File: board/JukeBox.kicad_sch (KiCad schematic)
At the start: 41 parts, among them J1 USB_C_Receptacle_USB2.0, J2 Conn_01x02, J3 Conn_01x04, J4 Conn_01x03, SW1 SW_SPST, SW10 SW_SPST, SW11 SW_SPST, SW12 SW_SPST, SW2 SW_SPST, SW3 SW_SPST, SW4 SW_SPST, SW5 SW_SPST, SW6 SW_SPST, SW7 SW_SPST, SW8 SW_SPST, SW9 SW_SPST, U1 ATmega8U2-A, Y1 16MHz

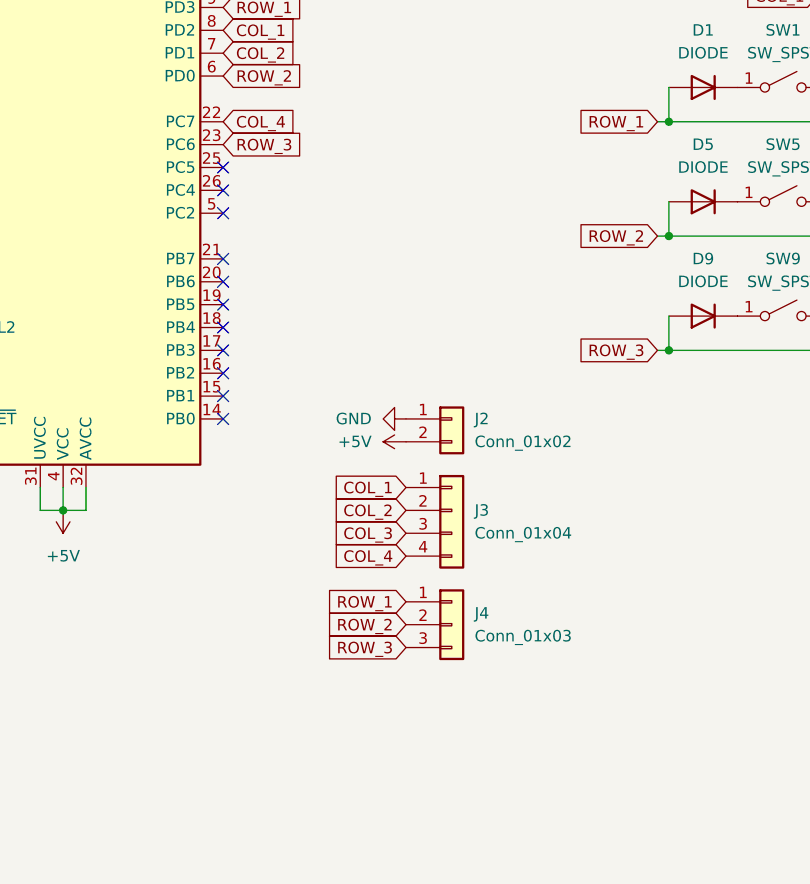
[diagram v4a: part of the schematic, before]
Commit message: add footprint for screen addon, change all tht components to smt
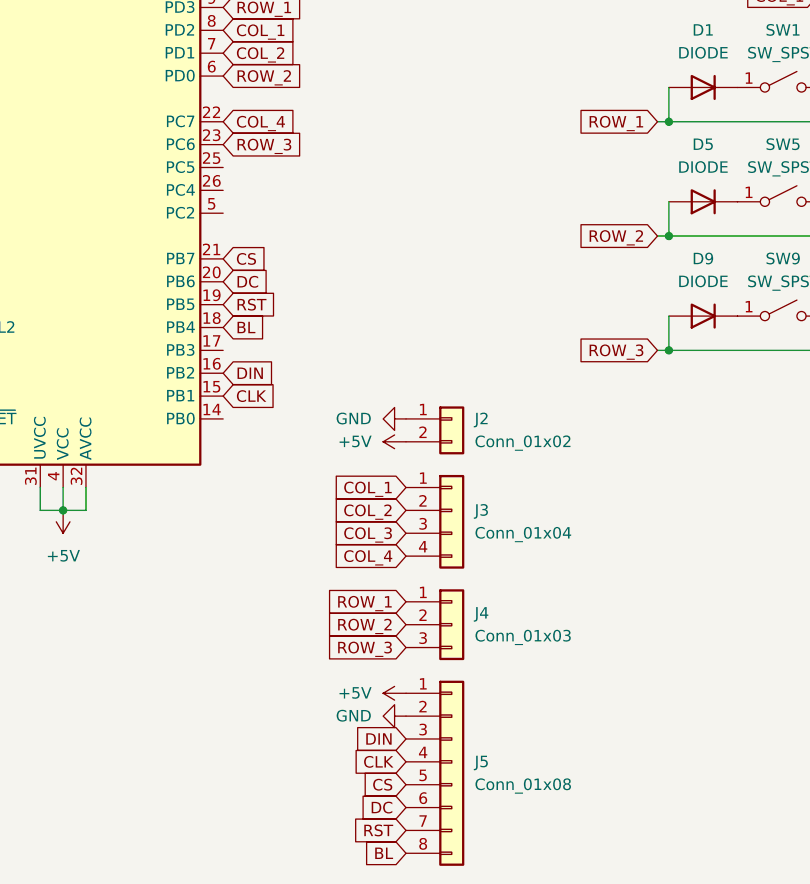
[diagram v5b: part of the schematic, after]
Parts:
- added J5: Conn_01x08, Connector_PinHeader_2.54mm:PinHeader_1x08_P2.54mm_Vertical, symbol Connector_Generic:Conn_01x08
- C1, C2, C3: footprint Capacitor_THT:C_Disc_D5.0mm_W2.5mm_P5.00mm -> Capacitor_SMD:C_1206_3216Metric_Pad1.33x1.80mm_HandSolder
- D1, D10, D11, D12, D2, D3, D4, D5, D6, D7, D8, D9: footprint Diode_THT:D_DO-15_P10.16mm_Horizontal -> Diode_SMD:D_1206_3216Metric_Pad1.42x1.75mm_HandSolder
- R1, R10, R11, R12, R2, R3, R4: footprint Resistor_THT:R_Axial_DIN0207_L6.3mm_D2.5mm_P10.16mm_Horizontal -> Resistor_SMD:R_1206_3216Metric_Pad1.30x1.75mm_HandSolder
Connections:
- net +5V: now also J5.1 (Pin_1)
- net GND: now also J5.2 (Pin_2)
- net CLK: now reaches U1.15 (PB1)
- net CLK: now also J5.4 (Pin_4)
- net DIN: now reaches U1.16 (PB2)
- net DIN: now also J5.3 (Pin_3)
- net BL: now reaches U1.18 (PB4)
- net BL: now also J5.8 (Pin_8)
- net RST: now reaches U1.19 (PB5)
- net RST: now also J5.7 (Pin_7)
- net DC: now reaches U1.20 (PB6)
- net DC: now also J5.6 (Pin_6)
- net CS: now reaches U1.21 (PB7)
- net CS: now also J5.5 (Pin_5)
- no-connect marks 16 -> 5

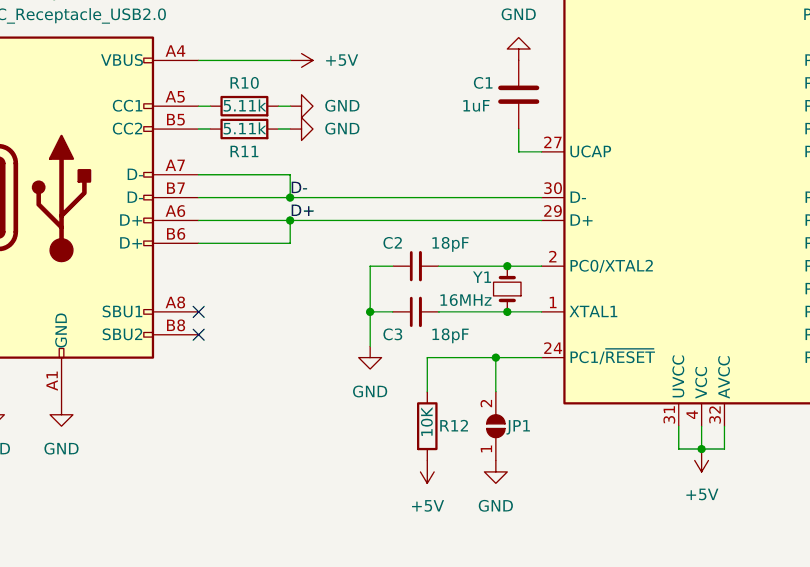
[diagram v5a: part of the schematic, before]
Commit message: add resistors to schematic, add mcu programming docs, add star to platformio stuff for atmega8u2
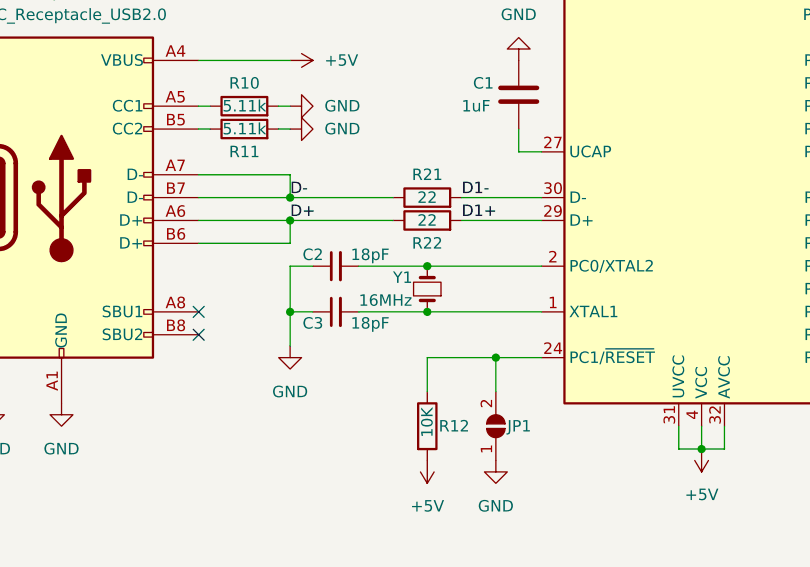
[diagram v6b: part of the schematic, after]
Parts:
- added R21, R22: 22, Resistor_SMD:R_1206_3216Metric_Pad1.30x1.75mm_HandSolder, symbol Device:R
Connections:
- net D+: now also R22.1; no longer U1.29 (D+)
- net D-: now also R21.1; no longer U1.30 (D-)
- new net D1+: R22.2, U1.29 (D+)
- new net D1-: R21.2, U1.30 (D-)
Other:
- moved on the sheet: C2, C3, Y1

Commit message: import rp2040 minimal kicad project
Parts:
- removed C2, C3: 18pF, Capacitor_SMD:C_1206_3216Metric_Pad1.33x1.80mm_HandSolder, symbol Device:C_Small
- removed D1, D10, D11, D12, D2, D3, D4, D5, D6, D7, D8, D9: DIODE, Diode_SMD:D_1206_3216Metric_Pad1.42x1.75mm_HandSolder, symbol Simulation_SPICE:DIODE
- removed J1: USB_C_Receptacle_USB2.0, jukebox-footprints:GCT_USB4085-GF-A_REVA4, symbol Connector:USB_C_Receptacle_USB2.0
- removed J3: Conn_01x04, Connector_PinHeader_2.54mm:PinHeader_1x04_P2.54mm_Vertical, symbol Connector_Generic:Conn_01x04
- removed J4: Conn_01x03, Connector_PinHeader_2.54mm:PinHeader_1x03_P2.54mm_Vertical, symbol Connector_Generic:Conn_01x03
- removed J5: Conn_01x08, Connector_PinHeader_2.54mm:PinHeader_1x08_P2.54mm_Vertical, symbol Connector_Generic:Conn_01x08
- removed JP1: (no value), Jumper:SolderJumper-2_P1.3mm_Open_Pad1.0x1.5mm, symbol Jumper:SolderJumper_2_Open
- removed R10, R11: 5.11k, Resistor_SMD:R_1206_3216Metric_Pad1.30x1.75mm_HandSolder, symbol Device:R
- removed R12: 10K, Resistor_SMD:R_1206_3216Metric_Pad1.30x1.75mm_HandSolder, symbol Device:R
- removed R21, R22: 22, Resistor_SMD:R_1206_3216Metric_Pad1.30x1.75mm_HandSolder, symbol Device:R
- removed SW1, SW10, SW11, SW12, SW2, SW3, SW4, SW5, SW6, SW7, SW8, SW9: SW_SPST, jukebox-footprints:Kailh_PG1350, symbol Switch:SW_SPST
- removed U1: ATmega8U2-A, Package_QFP:TQFP-32_7x7mm_P0.8mm, symbol MCU_Microchip_ATmega:ATmega8U2-A
- removed Y1: 16MHz, Crystal:Crystal_HC49-4H_Vertical, symbol Device:Crystal_Small
- added C10, C11, C12, C13, C14, C15, C16, C17, C2, C3, C4, C5, C6, C7, C8, C9: (no value), symbol Device:C
- added H1, H2, H3, H4: (no value), symbol Mechanical:MountingHole
- added J1: (no value), symbol Connector:USB_B_Micro
- added J3, J4: (no value), symbol Connector_Generic:Conn_02x18_Odd_Even
- added R5: (no value), symbol Device:R
- added U1: (no value), symbol Regulator_Linear:NCP1117-3.3_SOT223
- added U2: (no value), symbol Memory_Flash:W25Q128JVS
- added U3: (no value), symbol MCU_RaspberryPi_RP2040:RP2040
- added Y1: (no value), symbol Device:Crystal
- C1: value 1uF -> (none); footprint Capacitor_SMD:C_1206_3216Metric_Pad1.33x1.80mm_HandSolder -> (none)
- J2: value Conn_01x02 -> (none); footprint Connector_PinHeader_2.54mm:PinHeader_1x02_P2.54mm_Vertical -> (none)
- R1, R2, R3, R4: value 10k -> (none); footprint Resistor_SMD:R_1206_3216Metric_Pad1.30x1.75mm_HandSolder -> (none)
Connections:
- net +5V is gone; now on net GND: J2.2 (Pin_2)
- net GND: now also C1.2, C10.2, C11.2, C12.2, C13.2, C14.2, C15.2, C16.2, C17.2, C2.2, C3.2, C4.2, C5.2, C6.2, C7.2, C8.2, C9.2, J1.5 (GND), J1.6 (Shield), J3.1 (Pin_1), J3.11 (Pin_11), J3.13 (Pin_13), J3.15 (Pin_15), J3.17 (Pin_17), J3.19 (Pin_19), J3.21 (Pin_21), J3.23 (Pin_23), J3.25 (Pin_25), J3.27 (Pin_27), J3.29 (Pin_29), J3.3 (Pin_3), J3.31 (Pin_31), J3.33 (Pin_33), J3.35 (Pin_35), J3.36 (Pin_36), J3.5 (Pin_5), J3.7 (Pin_7), J3.9 (Pin_9), J4.10 (Pin_10), J4.12 (Pin_12), J4.14 (Pin_14), J4.16 (Pin_16), J4.18 (Pin_18), J4.2 (Pin_2), J4.20 (Pin_20), J4.22 (Pin_22), J4.24 (Pin_24), J4.26 (Pin_26), J4.28 (Pin_28), J4.30 (Pin_30), J4.32 (Pin_32), J4.34 (Pin_34), J4.35 (Pin_35), J4.36 (Pin_36), J4.4 (Pin_4), J4.6 (Pin_6), J4.8 (Pin_8), U1.1 (GND), U2.4 (GND), U3.19 (TESTEN), U3.57 (GND); no longer C1.1, J2.1 (Pin_1), R1.1, R2.1, R3.1, R4.1
- net COL_1 renamed ~{USB_BOOT}
- net ~{USB_BOOT}: now also J2.1 (Pin_1)
- net COL_2 renamed QSPI_SS
- net QSPI_SS: now also R1.1, U2.1 (~{CS}), U3.56 (QSPI_SS)
- net COL_3: no longer names the net of R3.2
- net COL_3: now also U3.47 (USB_DP)
- net COL_4: no longer names the net of R4.2
- net COL_4: now also U3.46 (USB_DM)
- new net: C3.1, R5.2, Y1.2
- new net +1V1: C6.1, C7.1, C8.1, U3.23 (DVDD), U3.45 (VREG_VOUT), U3.50 (DVDD)
- new net +3V3: C10.1, C11.1, C12.1, C13.1, C14.1, C15.1, C16.1, C17.1, C4.1, C5.1, C9.1, J3.2 (Pin_2), R2.1, U1.2 (VO), U2.8 (VCC), U3.1 (IOVDD), U3.10 (IOVDD), U3.22 (IOVDD), U3.33 (IOVDD), U3.42 (IOVDD), U3.43 (ADC_AVDD), U3.44 (VREG_IN), U3.48 (USB_VDD), U3.49 (IOVDD)
- new net GPIO0: J3.4 (Pin_4), U3.2 (GPIO0)
- new net GPIO1: J3.6 (Pin_6), U3.3 (GPIO1)
- new net GPIO10: J3.24 (Pin_24), U3.13 (GPIO10)
- new net GPIO11: J3.26 (Pin_26), U3.14 (GPIO11)
- new net GPIO12: J3.28 (Pin_28), U3.15 (GPIO12)
- new net GPIO13: J3.30 (Pin_30), U3.16 (GPIO13)
- new net GPIO14: J3.32 (Pin_32), U3.17 (GPIO14)
- new net GPIO15: J3.34 (Pin_34), U3.18 (GPIO15)
- new net GPIO16: J4.27 (Pin_27), U3.27 (GPIO16)
- new net GPIO17: J4.25 (Pin_25), U3.28 (GPIO17)
- new net GPIO18: J4.23 (Pin_23), U3.29 (GPIO18)
- new net GPIO19: J4.21 (Pin_21), U3.30 (GPIO19)
- new net GPIO2: J3.8 (Pin_8), U3.4 (GPIO2)
- new net GPIO20: J4.19 (Pin_19), U3.31 (GPIO20)
- new net GPIO21: J4.17 (Pin_17), U3.32 (GPIO21)
- new net GPIO22: J4.15 (Pin_15), U3.34 (GPIO22)
- new net GPIO23: J4.13 (Pin_13), U3.35 (GPIO23)
- new net GPIO24: J4.11 (Pin_11), U3.36 (GPIO24)
- new net GPIO25: J4.9 (Pin_9), U3.37 (GPIO25)
- new net GPIO26_ADC0: J4.7 (Pin_7), U3.38 (GPIO26_ADC0)
- new net GPIO27_ADC1: J4.5 (Pin_5), U3.39 (GPIO27_ADC1)
- new net GPIO28_ADC2: J4.3 (Pin_3), U3.40 (GPIO28_ADC2)
- new net GPIO29_ADC3: J4.1 (Pin_1), U3.41 (GPIO29_ADC3)
- new net GPIO3: J3.10 (Pin_10), U3.5 (GPIO3)
- new net GPIO4: J3.12 (Pin_12), U3.6 (GPIO4)
- new net GPIO5: J3.14 (Pin_14), U3.7 (GPIO5)
- new net GPIO6: J3.16 (Pin_16), U3.8 (GPIO6)
- new net GPIO7: J3.18 (Pin_18), U3.9 (GPIO7)
- new net GPIO8: J3.20 (Pin_20), U3.11 (GPIO8)
- new net GPIO9: J3.22 (Pin_22), U3.12 (GPIO9)
- new net QSPI_SCLK: U2.6 (CLK), U3.52 (QSPI_SCLK)
- new net QSPI_SD0: U2.5 (DI(IO0)), U3.53 (QSPI_SD0)
- new net QSPI_SD1: U2.2 (DO(IO1)), U3.55 (QSPI_SD1)
- new net QSPI_SD2: U2.3 (IO2), U3.54 (QSPI_SD2)
- new net QSPI_SD3: U2.7 (IO3), U3.51 (QSPI_SD3)
- new net RUN: J4.29 (Pin_29), U3.26 (RUN)
- new net SWCLK: J4.33 (Pin_33), U3.24 (SWCLK)
- new net SWD: J4.31 (Pin_31), U3.25 (SWD)
- new net USB_D+: J1.3 (D+), R3.1
- new net USB_D-: J1.2 (D-), R4.1
- new net VBUS: C1.1, J1.1 (VBUS), U1.3 (VI)
- new net XIN: C2.1, U3.20 (XIN), Y1.1
- new net XOUT: R5.1, U3.21 (XOUT)
- no-connect marks 5 -> 1
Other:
- note added: "Crystal"
- note added: "Flash"
- note added: "IOs"
- note added: "Make sure C10 is close to pin 44 of RP2040"
- note added: "Make sure C8 is close to pin 45 of RP2040"
- note added: "Make sure R3 and R4 are close to RP2040"
- note added: "Power"
- company: (none) -> Raspberry Pi (Trading) Ltd
- title: (none) -> RP2040 Minimal Design Example

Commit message: fix pinout, update schematic
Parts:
- removed C11, C12, C13, C14, C15, C16, C17, C9: (no value), symbol Device:C
- removed J2: (no value), symbol Connector_Generic:Conn_01x02
- removed J3, J4: (no value), symbol Connector_Generic:Conn_02x18_Odd_Even
- added D1, D10, D11, D12, D2, D3, D4, D5, D6, D7, D8, D9: DIODE, Diode_SMD:D_1206_3216Metric_Pad1.42x1.75mm_HandSolder, symbol Simulation_SPICE:DIODE
- added D13, D14, D15, D16, D17, D18, D19, D20, D21, D22, D23, D24: WS2812B, LED_SMD:LED_WS2812B_PLCC4_5.0x5.0mm_P3.2mm, symbol LED:WS2812B
- added J2, J6, J7: Conn_01x03, Connector_PinHeader_2.54mm:PinHeader_1x03_P2.54mm_Vertical, symbol Connector_Generic:Conn_01x03
- added J3: Conn_01x04, Connector_PinHeader_2.54mm:PinHeader_1x04_P2.54mm_Vertical, symbol Connector_Generic:Conn_01x04
- added J4: Conn_01x08, Connector_PinHeader_2.54mm:PinHeader_1x08_P2.54mm_Vertical, symbol Connector_Generic:Conn_01x08
- added J5: Conn_01x01, symbol Connector_Generic:Conn_01x01
- added JP1: SolderJumper_2_Open, symbol Jumper:SolderJumper_2_Open
- added R11, R12, R13, R14: 10k, Resistor_SMD:R_1206_3216Metric_Pad1.30x1.75mm_HandSolder, symbol Device:R
- added SW1, SW10, SW11, SW12, SW2, SW3, SW4, SW5, SW6, SW7, SW8, SW9: SW_SPST, jukebox-footprints:Kailh_PG1350, symbol Switch:SW_SPST
- C1, C4: value (none) -> 10u; footprint (none) -> Capacitor_SMD:C_0805_2012Metric
- C10, C8: value (none) -> 1u; footprint (none) -> Capacitor_SMD:C_0402_1005Metric
- C2, C3: value (none) -> 27p; footprint (none) -> Capacitor_SMD:C_0402_1005Metric
- C5, C6, C7: value (none) -> 100n; footprint (none) -> Capacitor_SMD:C_0402_1005Metric
- H1, H2, H3, H4: value (none) -> MountingHole; footprint (none) -> MountingHole:MountingHole_2.7mm_M2.5
- J1: value (none) -> USB_B_Micro; footprint (none) -> RP2040_minimal:USB_Micro-B_Amphenol_10103594-0001LF_Horizontal_modified
- R1, R5: value (none) -> 1k; footprint (none) -> Capacitor_SMD:C_0402_1005Metric
- R2: value (none) -> DNF; footprint (none) -> Capacitor_SMD:C_0402_1005Metric
- R3, R4: value (none) -> 27; footprint (none) -> Capacitor_SMD:C_0402_1005Metric
- U1: value (none) -> NCP1117-3.3_SOT223; footprint (none) -> Package_TO_SOT_SMD:SOT-223-3_TabPin2
- U2: value (none) -> W25Q128JVS; footprint (none) -> Package_SO:SOIC-8_5.23x5.23mm_P1.27mm
- U3: value (none) -> RP2040; footprint (none) -> RP2040_minimal:RP2040-QFN-56
- Y1: value (none) -> ABLS-12.000MHZ-B4-T; footprint (none) -> RP2040_minimal:Crystal_SMD_HC49-US
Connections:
- net +3V3: now also D13.1 (VDD), D14.1 (VDD), D15.1 (VDD), D16.1 (VDD), D17.1 (VDD), D18.1 (VDD), D19.1 (VDD), D20.1 (VDD), D21.1 (VDD), D22.1 (VDD), D23.1 (VDD), D24.1 (VDD), J4.1 (Pin_1)
- net GND: now also D13.3 (VSS), D14.3 (VSS), D15.3 (VSS), D16.3 (VSS), D17.3 (VSS), D18.3 (VSS), D19.3 (VSS), D20.3 (VSS), D21.3 (VSS), D22.3 (VSS), D23.3 (VSS), D24.3 (VSS), J4.2 (Pin_2), J6.2 (Pin_2), J7.2 (Pin_2), JP1.1 (A), R11.1, R12.1, R13.1, R14.1
- net GPIO10: now also J4.5 (Pin_5)
- net GPIO11: now also J4.6 (Pin_6)
- net GPIO12: now also J4.7 (Pin_7)
- net GPIO13: now also J4.8 (Pin_8)
- net GPIO15: now also D13.4 (DIN), J5.1 (Pin_1)
- net GPIO16: now also D1.1 (A), D2.1 (A), D3.1 (A), D4.1 (A), J2.1 (Pin_1)
- net GPIO17: now also D5.1 (A), D6.1 (A), D7.1 (A), D8.1 (A), J2.2 (Pin_2)
- net GPIO18: now also D10.1 (A), D11.1 (A), D12.1 (A), D9.1 (A), J2.3 (Pin_3)
- net GPIO19: now also J3.1 (Pin_1), R11.2, SW1.2 (B), SW5.2 (B), SW9.2 (B)
- net GPIO20: now also J3.2 (Pin_2), R12.2, SW10.2 (B), SW2.2 (B), SW6.2 (B)
- net GPIO21: now also J3.3 (Pin_3), R13.2, SW11.2 (B), SW3.2 (B), SW7.2 (B)
- net GPIO22: now also J3.4 (Pin_4), R14.2, SW12.2 (B), SW4.2 (B), SW8.2 (B)
- net GPIO8: now also J4.3 (Pin_3)
- net GPIO9: now also J4.4 (Pin_4)
- net ~{USB_BOOT}: now also JP1.2 (B)
- net GPIO0 renamed DBGRX
- net DBGRX: now also J6.1 (Pin_1)
- net GPIO1 renamed DBGTX
- net DBGTX: now also J6.3 (Pin_3)
- net SWCLK renamed DBGSC
- net DBGSC: now also J7.1 (Pin_1)
- net SWD renamed DBGSD
- net DBGSD: now also J7.3 (Pin_3)
- new net: D11.2 (K), SW11.1 (A)
- new net: D7.2 (K), SW7.1 (A)
- new net: D9.2 (K), SW9.1 (A)
- new net: D21.2 (DOUT), D22.4 (DIN)
- new net: D20.2 (DOUT), D21.4 (DIN)
- new net: D4.2 (K), SW4.1 (A)
- new net: D8.2 (K), SW8.1 (A)
- new net: D10.2 (K), SW10.1 (A)
- new net: D19.2 (DOUT), D20.4 (DIN)
- new net: D18.2 (DOUT), D19.4 (DIN)
- new net: D2.2 (K), SW2.1 (A)
- new net: D3.2 (K), SW3.1 (A)
- new net: D6.2 (K), SW6.1 (A)
- new net: D16.2 (DOUT), D17.4 (DIN)
- new net: D15.2 (DOUT), D16.4 (DIN)
- new net: D17.2 (DOUT), D18.4 (DIN)
- new net: D23.2 (DOUT), D24.4 (DIN)
- new net: D22.2 (DOUT), D23.4 (DIN)
- new net: D1.2 (K), SW1.1 (A)
- new net: D5.2 (K), SW5.1 (A)
- new net: D13.2 (DOUT), D14.4 (DIN)
- new net: D14.2 (DOUT), D15.4 (DIN)
- new net: D12.2 (K), SW12.1 (A)
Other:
- note added: "Keyboard"
- note added: "Microcontroller"
- note added: "Mounting"
- note added: "RGB LEDs"
- moved on the sheet: C1, C10, C2, C3, C4, C5, C6, C7, C8, H1, H2, H3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
